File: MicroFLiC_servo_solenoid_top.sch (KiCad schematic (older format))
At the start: 9 parts, among them P1 1x14 socket strip, P2 1x14 header strip, P3 Jack_3.5mm_3pin, P4 Jack_3.5mm_3pin, P5 RCA_3, P6 RCA_3, P7 1x6 header strip, P8 1x4 header strip, P9 1x4 socket strip

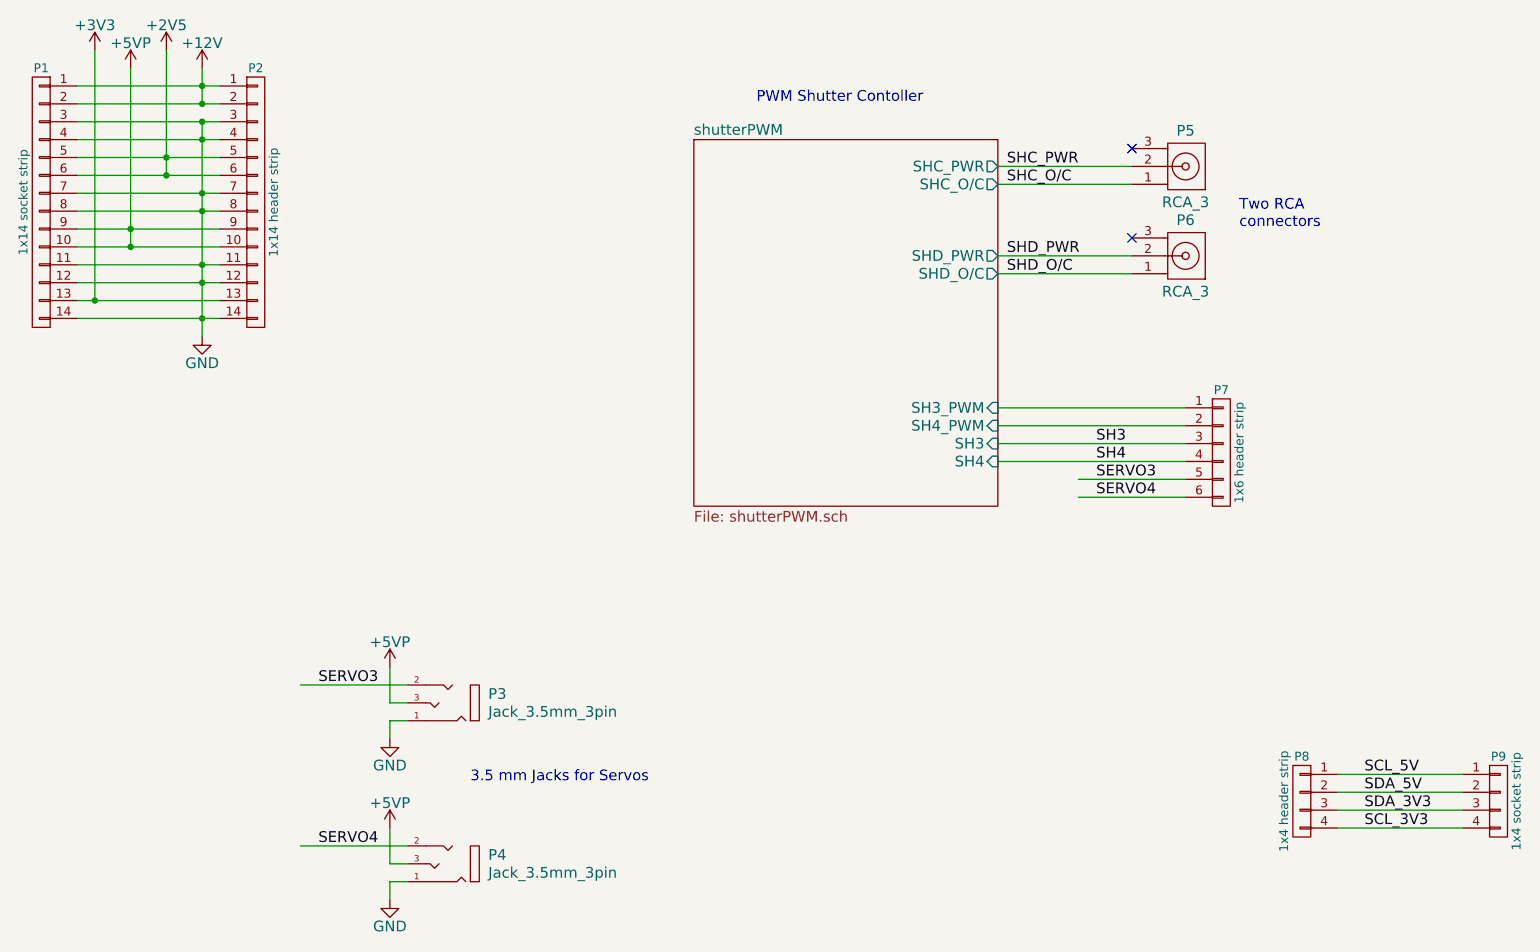
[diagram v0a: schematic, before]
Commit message: Added better de-bouncing diode description
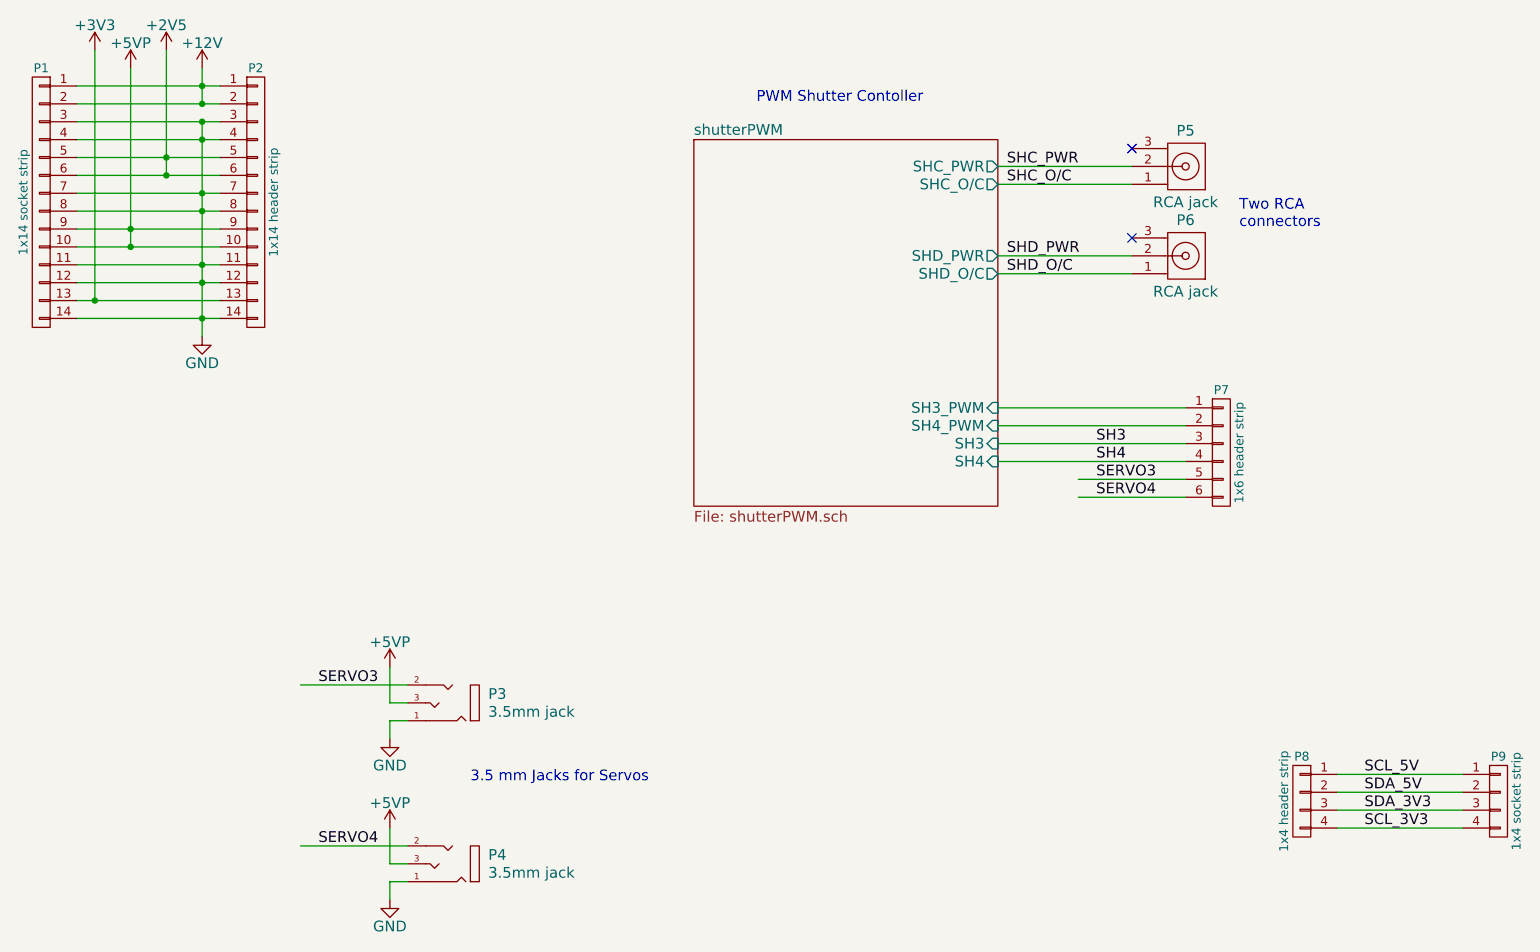
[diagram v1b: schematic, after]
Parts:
- P3, P4: value Jack_3.5mm_3pin -> 3.5mm jack; Alt. Order Code (none) -> N/A
- P5, P6: value RCA_3 -> RCA jack; Alt. Order Code (none) -> N/A
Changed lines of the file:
@@
 P 3550 4700
 F 0 "P3" H 3300 4700 60  0000 R CNN
-F 1 "Jack_3.5mm_3pin" H 3300 4800 60  0000 R CNN
+F 1 "3.5mm jack" H 3300 4800 60  0000 R CNN
 F 2 "jakub:MJ4435-R" H 3525 4700 60  0001 C CNN
 F 3 "" H 3525 4700 60  0000 C CNN
@@
 F 8 "1638670" H 3550 4700 60  0001 C CNN "Order Code"
 F 9 "N/A" H 3550 4700 60  0001 C CNN "Alt. Supplier"
-F 10 "Right-angle SMD 3.5mm 3-pin jack" H 3550 4700 60  0001 C CNN "Note"
+F 10 "N/A" H 3550 4700 60  0001 C CNN "Alt. Order Code"
+F 11 "Right-angle SMD 3.5mm 3-pin jack" H 3550 4700 60  0001 C CNN "Note"
 	1    3550 4700
 	-1   0    0    1
@@
 P 7700 2250
 F 0 "P6" H 7700 2450 60  0000 C CNN
-F 1 "RCA_3" H 7700 2050 60  0000 C CNN
+F 1 "RCA jack" H 7700 2050 60  0000 C CNN
 F 2 "jakub:PSG01544" H 7700 2250 60  0001 C CNN
 F 3 "" H 7700 2250 60  0000 C CNN
@@
 F 8 "1280698" H 7700 2250 60  0001 C CNN "Order Code"
 F 9 "N/A" H 7700 2250 60  0001 C CNN "Alt. Supplier"
-F 10 "Right-angle RCA jack" H 7700 2250 60  0001 C CNN "Note"
+F 10 "N/A" H 7700 2250 60  0001 C CNN "Alt. Order Code"
+F 11 "Right-angle RCA jack" H 7700 2250 60  0001 C CNN "Note"
 	1    7700 2250
 	1    0    0    -1
@@
 P 7700 1750
 F 0 "P5" H 7700 1950 60  0000 C CNN
-F 1 "RCA_3" H 7700 1550 60  0000 C CNN
+F 1 "RCA jack" H 7700 1550 60  0000 C CNN
 F 2 "jakub:PSG01544" H 7700 1750 60  0001 C CNN
 F 3 "" H 7700 1750 60  0000 C CNN
@@
 F 8 "1280698" H 7700 1750 60  0001 C CNN "Order Code"
 F 9 "N/A" H 7700 1750 60  0001 C CNN "Alt. Supplier"
-F 10 "Right-angle RCA jack" H 7700 1750 60  0001 C CNN "Note"
+F 10 "N/A" H 7700 1750 60  0001 C CNN "Alt. Order Code"
+F 11 "Right-angle RCA jack" H 7700 1750 60  0001 C CNN "Note"
 	1    7700 1750
 	1    0    0    -1
@@
 P 3550 5600
 F 0 "P4" H 3300 5600 60  0000 R CNN
-F 1 "Jack_3.5mm_3pin" H 3300 5700 60  0000 R CNN
+F 1 "3.5mm jack" H 3300 5700 60  0000 R CNN
 F 2 "jakub:MJ4435-R" H 3525 5600 60  0001 C CNN
 F 3 "" H 3525 5600 60  0000 C CNN
@@
 F 8 "1638670" H 3550 5600 60  0001 C CNN "Order Code"
 F 9 "N/A" H 3550 5600 60  0001 C CNN "Alt. Supplier"
-F 10 "Right-angle SMD 3.5mm 3-pin jack" H 3550 5600 60  0001 C CNN "Note"
+F 10 "N/A" H 3550 5600 60  0001 C CNN "Alt. Order Code"
+F 11 "Right-angle SMD 3.5mm 3-pin jack" H 3550 5600 60  0001 C CNN "Note"
 	1    3550 5600
 	-1   0    0    1
